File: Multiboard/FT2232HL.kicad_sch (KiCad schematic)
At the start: 41 parts, among them J5 Conn_01x06_Socket, U4 FT2232HL-REEL, U5 93LCxxC, Y3 12MHz

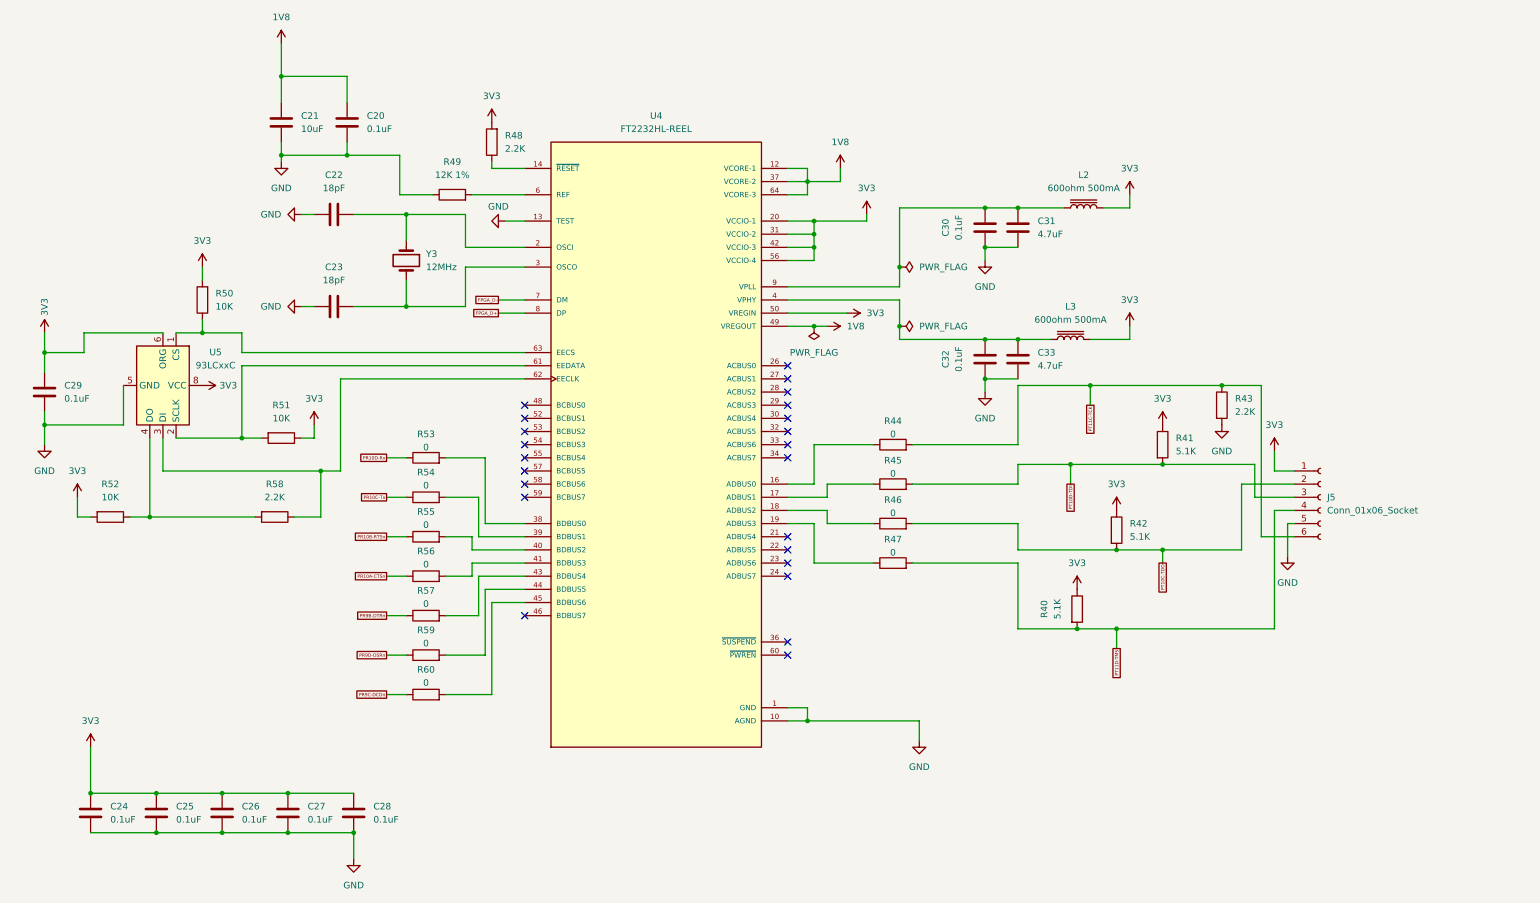
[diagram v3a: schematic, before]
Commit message: synchronised sch and pcb. Added jtag connection between fpga and ftdi
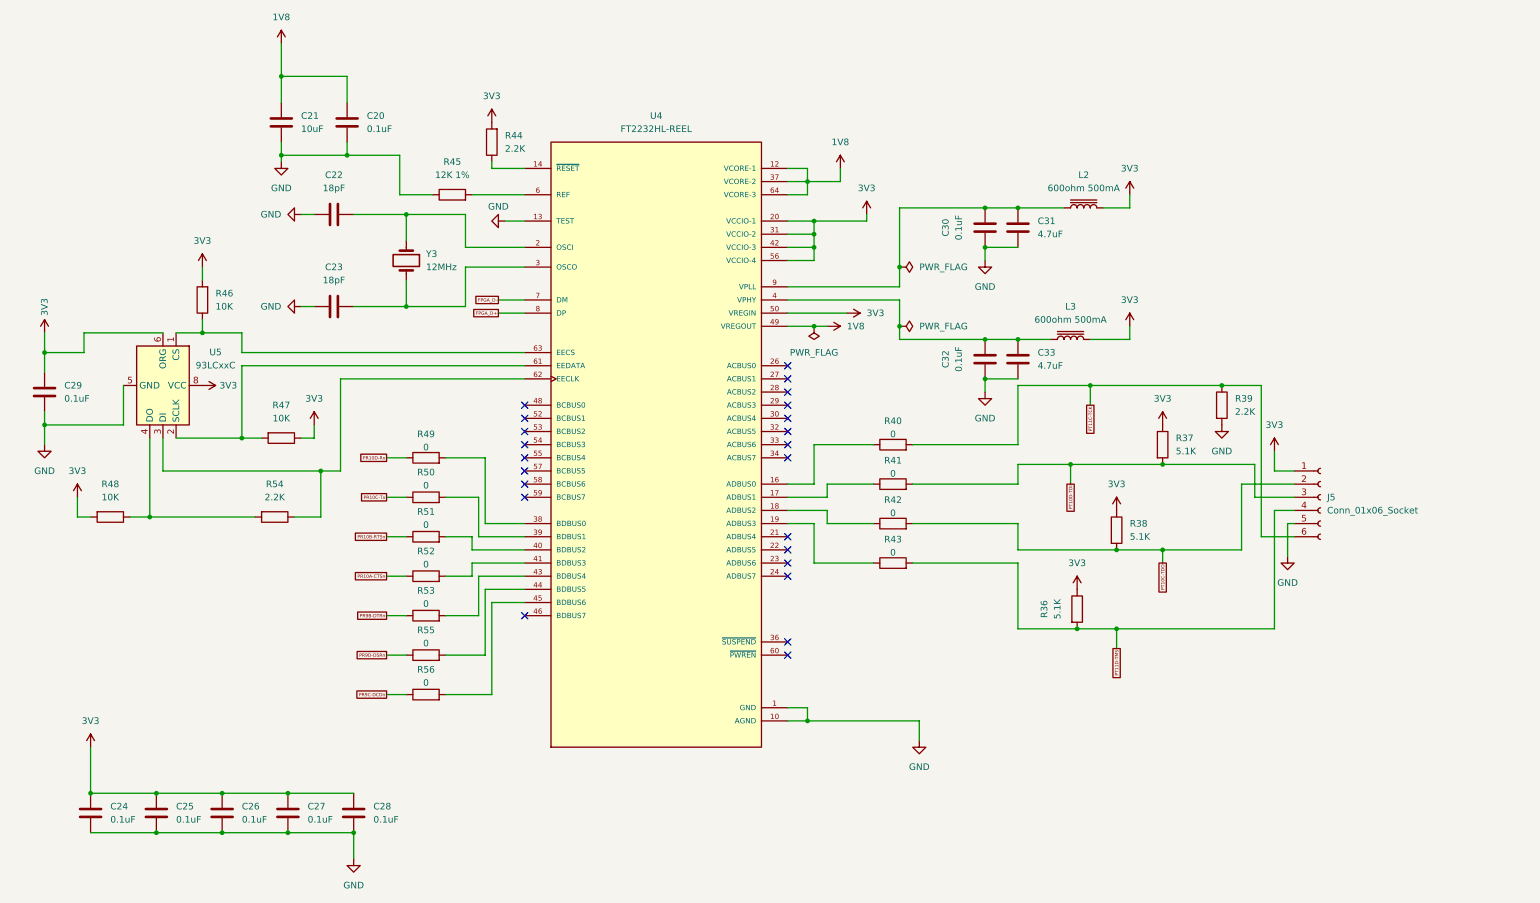
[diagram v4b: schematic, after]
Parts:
- J5: footprint Connector_JST:JST_EH_S6B-EH_1x06_P2.50mm_Horizontal -> Connector_Hirose:Hirose_DF13-06P-1.25DSA_1x06_P1.25mm_Vertical
- renumbered R40 to R36, R41 to R37, R42 to R38, R43 to R39, R44 to R40, R45 to R41, R46 to R42, R47 to R43, R48 to R44, R49 to R45, R50 to R46, R51 to R47, R52 to R48, R53 to R49, R54 to R50, R55 to R51, R56 to R52, R57 to R53, R58 to R54, R59 to R55, R60 to R56
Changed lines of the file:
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@@
 		(on_board yes)
 		(dnp no)
-		(property "Reference" "R55"
+		(property "Reference" "R51"
 			(at 91.44 110.744 90)
 			(effects
@@
 			(project "Multiboard"
 				(path "/9ed4a389-3aa7-41f1-b239-280eb7f09ef1/a1879700-d4ae-4f4f-b9ed-53e5618d969d/39699ff7-0a15-4f77-94a0-c1dca93517d8"
-					(reference "R55")
+					(reference "R51")
 					(unit 1)
 				)
@@
 		(on_board yes)
 		(dnp no)
-		(property "Reference" "R40"
+		(property "Reference" "R36"
 			(at 210.82 129.54 90)
 			(effects
@@
 			(project "Multiboard"
 				(path "/9ed4a389-3aa7-41f1-b239-280eb7f09ef1/a1879700-d4ae-4f4f-b9ed-53e5618d969d/39699ff7-0a15-4f77-94a0-c1dca93517d8"
-					(reference "R40")
+					(reference "R36")
 					(unit 1)
 				)
@@
 		(dnp no)
 		(fields_autoplaced yes)
-		(property "Reference" "R49"
+		(property "Reference" "R45"
 			(at 96.52 43.18 90)
 			(effects
@@
 			(project ""
 				(path "/9ed4a389-3aa7-41f1-b239-280eb7f09ef1/a1879700-d4ae-4f4f-b9ed-53e5618d969d/39699ff7-0a15-4f77-94a0-c1dca93517d8"
-					(reference "R49")
+					(reference "R45")
 					(unit 1)
 				)
@@
 		(on_board yes)
 		(dnp no)
-		(property "Reference" "R60"
+		(property "Reference" "R56"
 			(at 91.44 141.224 90)
 			(effects
@@
 			(project "Multiboard"
 				(path "/9ed4a389-3aa7-41f1-b239-280eb7f09ef1/a1879700-d4ae-4f4f-b9ed-53e5618d969d/39699ff7-0a15-4f77-94a0-c1dca93517d8"
-					(reference "R60")
+					(reference "R56")
 					(unit 1)
 				)
@@
 		(dnp no)
 		(fields_autoplaced yes)
-		(property "Reference" "R50"
+		(property "Reference" "R46"
 			(at 50.8 68.5799 0)
 			(effects
@@
 			(project "Multiboard"
 				(path "/9ed4a389-3aa7-41f1-b239-280eb7f09ef1/a1879700-d4ae-4f4f-b9ed-53e5618d969d/39699ff7-0a15-4f77-94a0-c1dca93517d8"
-					(reference "R50")
+					(reference "R46")
 					(unit 1)
 				)
@@
 			)
 		)
-		(property "Footprint" "Connector_JST:JST_EH_S6B-EH_1x06_P2.50mm_Horizontal"
+		(property "Footprint" "Connector_Hirose:Hirose_DF13-06P-1.25DSA_1x06_P1.25mm_Vertical"
 			(at 264.16 107.95 0)
 			(effects
@@
 		(on_board yes)
 		(dnp no)
-		(property "Reference" "R47"
+		(property "Reference" "R43"
 			(at 181.61 116.078 90)
 			(effects
@@
 			(project "Multiboard"
 				(path "/9ed4a389-3aa7-41f1-b239-280eb7f09ef1/a1879700-d4ae-4f4f-b9ed-53e5618d969d/39699ff7-0a15-4f77-94a0-c1dca93517d8"
-					(reference "R47")
+					(reference "R43")
 					(unit 1)
 				)
@@
 		(dnp no)
 		(fields_autoplaced yes)
-		(property "Reference" "R43"
+		(property "Reference" "R39"
 			(at 247.65 88.8999 0)
 			(effects
@@
 			(project "Multiboard"
 				(path "/9ed4a389-3aa7-41f1-b239-280eb7f09ef1/a1879700-d4ae-4f4f-b9ed-53e5618d969d/39699ff7-0a15-4f77-94a0-c1dca93517d8"
-					(reference "R43")
+					(reference "R39")
 					(unit 1)
 				)
@@
 		(on_board yes)
 		(dnp no)
-		(property "Reference" "R54"
+		(property "Reference" "R50"
 			(at 91.44 103.124 90)
 			(effects
@@
 			(project "Multiboard"
 				(path "/9ed4a389-3aa7-41f1-b239-280eb7f09ef1/a1879700-d4ae-4f4f-b9ed-53e5618d969d/39699ff7-0a15-4f77-94a0-c1dca93517d8"
-					(reference "R54")
+					(reference "R50")
 					(unit 1)
 				)
@@
 		(on_board yes)
 		(dnp no)
-		(property "Reference" "R53"
+		(property "Reference" "R49"
 			(at 91.44 95.758 90)
 			(effects
@@
 			(project "Multiboard"
 				(path "/9ed4a389-3aa7-41f1-b239-280eb7f09ef1/a1879700-d4ae-4f4f-b9ed-53e5618d969d/39699ff7-0a15-4f77-94a0-c1dca93517d8"
-					(reference "R53")
+					(reference "R49")
 					(unit 1)
 				)
@@
 		(dnp no)
 		(fields_autoplaced yes)
-		(property "Reference" "R58"
+		(property "Reference" "R54"
 			(at 62.23 105.41 90)
 			(effects
@@
 			(project "Multiboard"
 				(path "/9ed4a389-3aa7-41f1-b239-280eb7f09ef1/a1879700-d4ae-4f4f-b9ed-53e5618d969d/39699ff7-0a15-4f77-94a0-c1dca93517d8"
-					(reference "R58")
+					(reference "R54")
 					(unit 1)
 				)
@@
 		(on_board yes)
 		(dnp no)
-		(property "Reference" "R56"
+		(property "Reference" "R52"
 			(at 91.44 118.364 90)
 			(effects
@@
 			(project "Multiboard"
 				(path "/9ed4a389-3aa7-41f1-b239-280eb7f09ef1/a1879700-d4ae-4f4f-b9ed-53e5618d969d/39699ff7-0a15-4f77-94a0-c1dca93517d8"
-					(reference "R56")
+					(reference "R52")
 					(unit 1)
 				)
@@
 		(on_board yes)
 		(dnp no)
-		(property "Reference" "R46"
+		(property "Reference" "R42"
 			(at 181.61 108.458 90)
 			(effects
@@
 			(project "Multiboard"
 				(path "/9ed4a389-3aa7-41f1-b239-280eb7f09ef1/a1879700-d4ae-4f4f-b9ed-53e5618d969d/39699ff7-0a15-4f77-94a0-c1dca93517d8"
-					(reference "R46")
+					(reference "R42")
 					(unit 1)
 				)
@@
 		(on_board yes)
 		(dnp no)
-		(property "Reference" "R44"
+		(property "Reference" "R40"
 			(at 181.61 93.218 90)
 			(effects
@@
 			(project "Multiboard"
 				(path "/9ed4a389-3aa7-41f1-b239-280eb7f09ef1/a1879700-d4ae-4f4f-b9ed-53e5618d969d/39699ff7-0a15-4f77-94a0-c1dca93517d8"
-					(reference "R44")
+					(reference "R40")
 					(unit 1)
 				)
@@
 		(dnp no)
 		(fields_autoplaced yes)
-		(property "Reference" "R51"
+		(property "Reference" "R47"
 			(at 63.5 90.17 90)
 			(effects
@@
 			(project "Multiboard"
 				(path "/9ed4a389-3aa7-41f1-b239-280eb7f09ef1/a1879700-d4ae-4f4f-b9ed-53e5618d969d/39699ff7-0a15-4f77-94a0-c1dca93517d8"
-					(reference "R51")
+					(reference "R47")
 					(unit 1)
 				)
@@
 		(on_board yes)
 		(dnp no)
-		(property "Reference" "R59"
+		(property "Reference" "R55"
 			(at 91.44 133.604 90)
 			(effects
@@
 			(project "Multiboard"
 				(path "/9ed4a389-3aa7-41f1-b239-280eb7f09ef1/a1879700-d4ae-4f4f-b9ed-53e5618d969d/39699ff7-0a15-4f77-94a0-c1dca93517d8"
-					(reference "R59")
+					(reference "R55")
 					(unit 1)
 				)
@@
 		(on_board yes)
 		(dnp no)
-		(property "Reference" "R45"
+		(property "Reference" "R41"
 			(at 181.61 100.838 90)
 			(effects
@@
 			(project "Multiboard"
 				(path "/9ed4a389-3aa7-41f1-b239-280eb7f09ef1/a1879700-d4ae-4f4f-b9ed-53e5618d969d/39699ff7-0a15-4f77-94a0-c1dca93517d8"
-					(reference "R45")
+					(reference "R41")
 					(unit 1)
 				)
@@
 		(dnp no)
 		(fields_autoplaced yes)
-		(property "Reference" "R41"
+		(property "Reference" "R37"
 			(at 236.22 96.5199 0)
 			(effects
@@
 			(project "Multiboard"
 				(path "/9ed4a389-3aa7-41f1-b239-280eb7f09ef1/a1879700-d4ae-4f4f-b9ed-53e5618d969d/39699ff7-0a15-4f77-94a0-c1dca93517d8"
-					(reference "R41")
+					(reference "R37")
 					(unit 1)
 				)
@@
 		(dnp no)
 		(fields_autoplaced yes)
-		(property "Reference" "R48"
+		(property "Reference" "R44"
 			(at 106.68 38.0999 0)
 			(effects
@@
 			(project ""
 				(path "/9ed4a389-3aa7-41f1-b239-280eb7f09ef1/a1879700-d4ae-4f4f-b9ed-53e5618d969d/39699ff7-0a15-4f77-94a0-c1dca93517d8"
-					(reference "R48")
+					(reference "R44")
 					(unit 1)
 				)
@@
 		(on_board yes)
 		(dnp no)
-		(property "Reference" "R57"
+		(property "Reference" "R53"
 			(at 91.44 125.984 90)
 			(effects
@@
 			(project "Multiboard"
 				(path "/9ed4a389-3aa7-41f1-b239-280eb7f09ef1/a1879700-d4ae-4f4f-b9ed-53e5618d969d/39699ff7-0a15-4f77-94a0-c1dca93517d8"
-					(reference "R57")
+					(reference "R53")
 					(unit 1)
 				)
@@
 		(dnp no)
 		(fields_autoplaced yes)
-		(property "Reference" "R52"
+		(property "Reference" "R48"
 			(at 30.48 105.41 90)
 			(effects
@@
 			(project "Multiboard"
 				(path "/9ed4a389-3aa7-41f1-b239-280eb7f09ef1/a1879700-d4ae-4f4f-b9ed-53e5618d969d/39699ff7-0a15-4f77-94a0-c1dca93517d8"
-					(reference "R52")
+					(reference "R48")
 					(unit 1)
 				)
@@
 		(dnp no)
 		(fields_autoplaced yes)
-		(property "Reference" "R42"
+		(property "Reference" "R38"
 			(at 227.33 113.0299 0)
 			(effects
@@
 			(project "Multiboard"
 				(path "/9ed4a389-3aa7-41f1-b239-280eb7f09ef1/a1879700-d4ae-4f4f-b9ed-53e5618d969d/39699ff7-0a15-4f77-94a0-c1dca93517d8"
-					(reference "R42")
+					(reference "R38")
 					(unit 1)
 				)

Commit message: cleared part of errors and warnings
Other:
- company: (none) -> Technological School "Electronic Systems"
- title: (none) -> IR-Multiboard/FPGA_FTDI
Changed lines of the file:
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@@
 	(generator_version "9.0")
 	(paper "A4")
+	(title_block
+		(title "IR-Multiboard/FPGA_FTDI")
+		(date "2026-02-23")
+		(company "Technological School \"Electronic Systems\"")
+	)
 	(junction
 		(at 199.39 77.47)

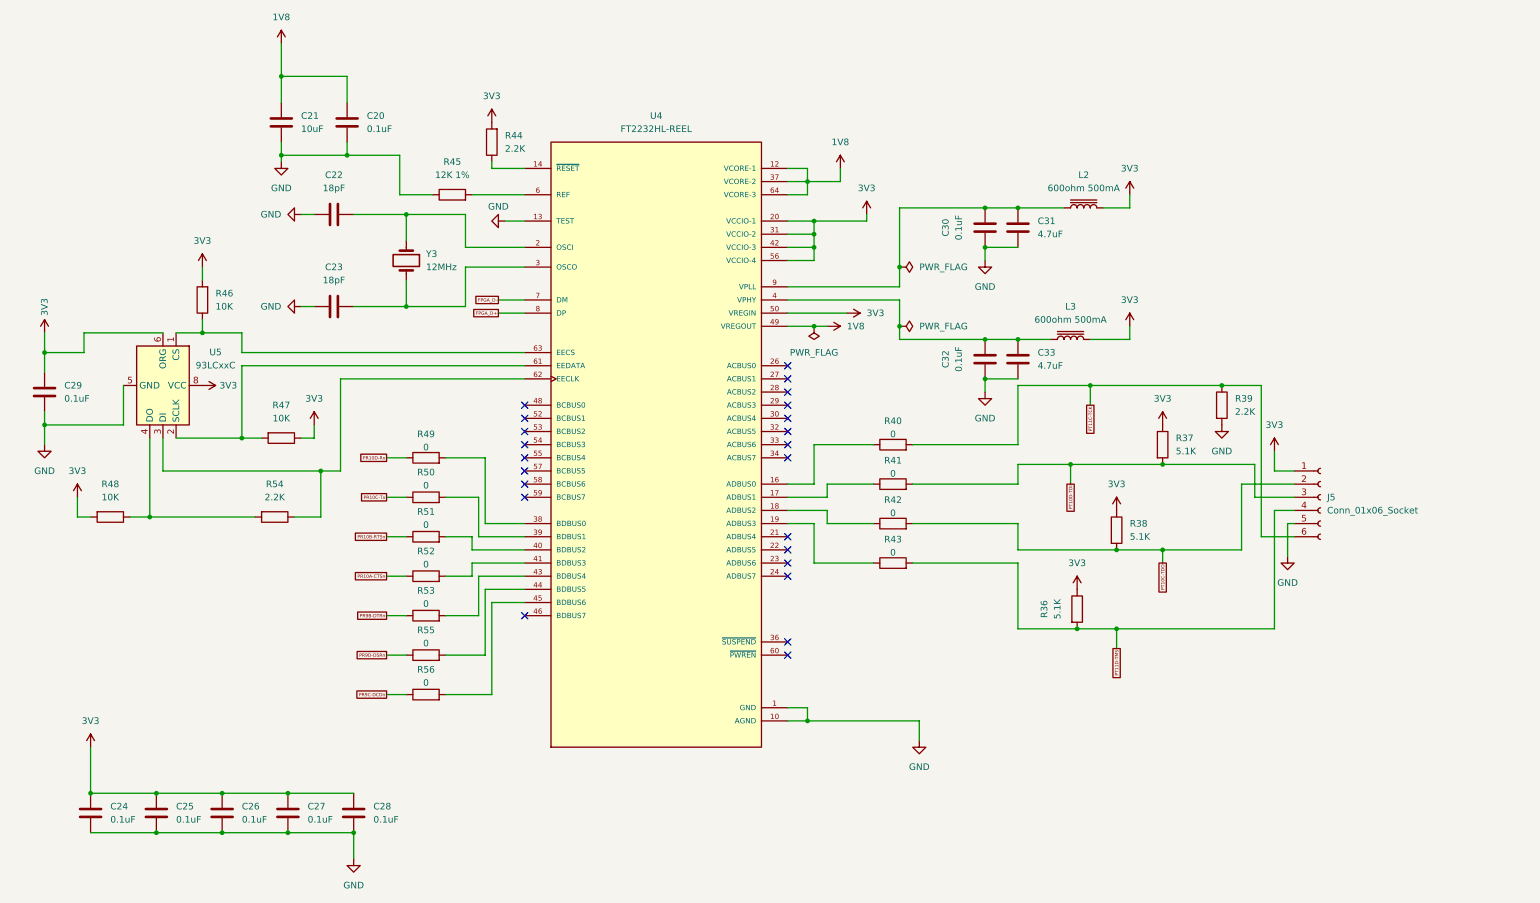
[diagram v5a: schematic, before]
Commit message: fixed dead copper zones and cleared all errors
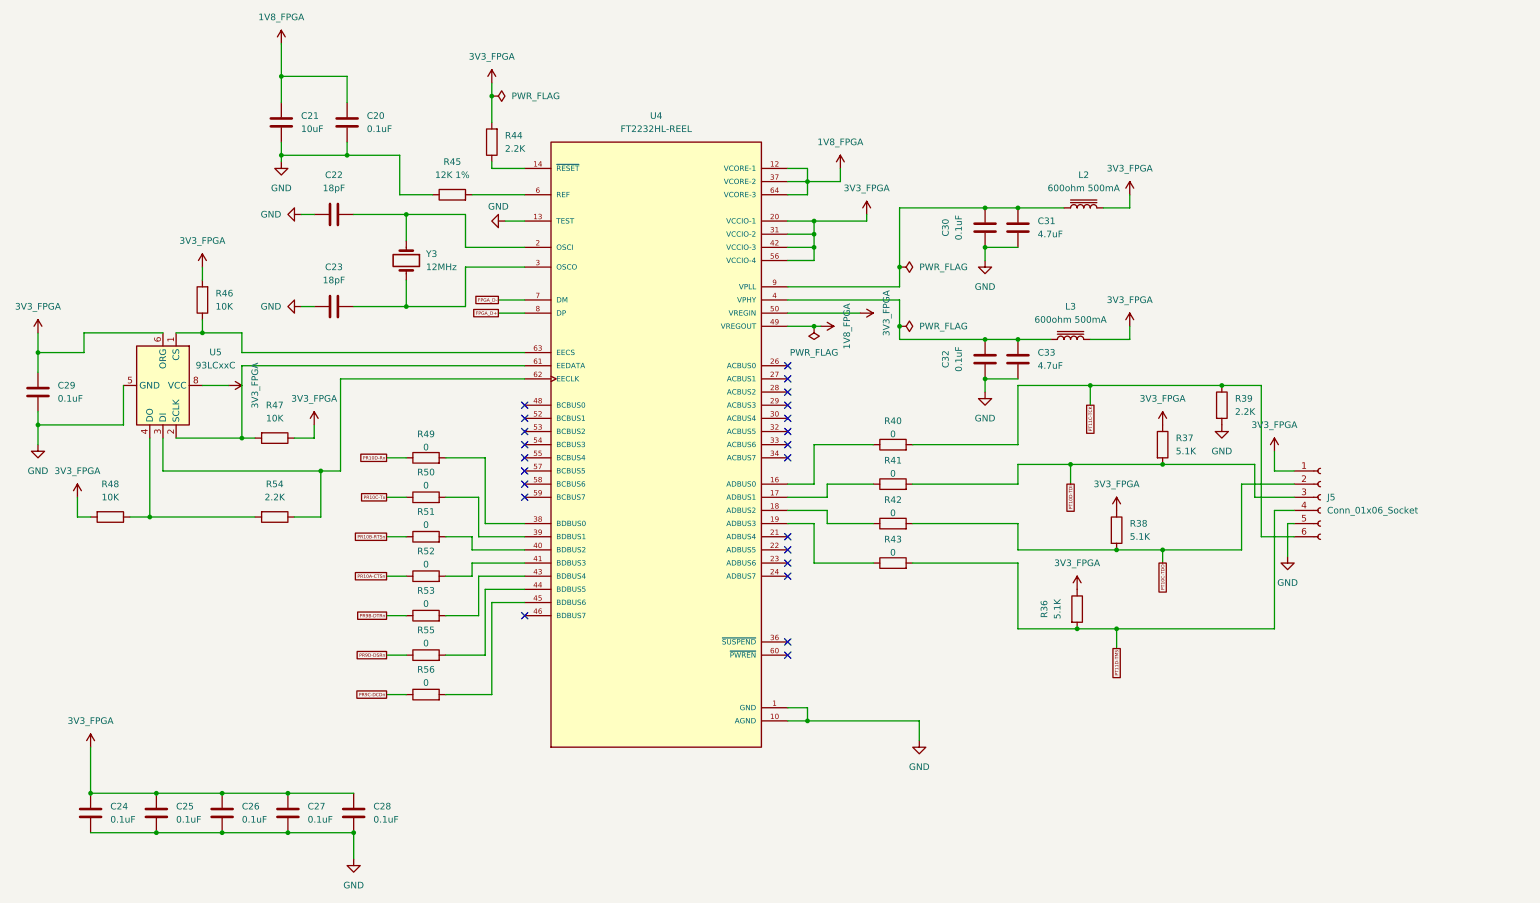
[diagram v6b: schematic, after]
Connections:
- net 1V8 renamed 1V8_FPGA
- net 3V3 renamed 3V3_FPGA
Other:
- moved on the sheet: C29, R47

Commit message: Generated BOM
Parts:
- C20, C24, C25, C26, C27, C28, C29, C30, C32: LCSC Part Number (none) -> C14663
- C21: LCSC Part Number (none) -> C19702
- C22, C23: LCSC Part Number (none) -> C49326300
- C31, C33: LCSC Part Number (none) -> C19666
- L2, L3: LCSC Part Number (none) -> C20345
- R36, R37, R38: LCSC Part Number (none) -> C2907044
- R39, R44, R54: LCSC Part Number (none) -> C114662
- R40, R41, R42, R43, R49, R50, R51, R52, R53, R55, R56: LCSC Part Number (none) -> C95177
- R45: LCSC Part Number (none) -> C431727
- R46, R47, R48: LCSC Part Number (none) -> C98220
- U4: LCSC Part Number (none) -> C27882
- U5: LCSC Part Number (none) -> C1350395

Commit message: Restored older version due to KiCAD glitching
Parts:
- U5: LCSC Part Number C1350395 -> (none)
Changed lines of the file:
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@@
 		(exclude_from_sim no)
 		(in_bom yes)
-		(on_board no)
+		(on_board yes)
 		(dnp no)
 		(property "Reference" "Y3"
@@
 			)
 		)
-		(property "LCSC Part Number" "C1350395"
+		(property "LCSC Part Number" ""
 			(at 40.64 86.36 90)
 			(effects
